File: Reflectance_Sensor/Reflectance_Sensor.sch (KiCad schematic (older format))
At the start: 9 parts, among them Q1 Phototransistor, Q2 Phototransistor

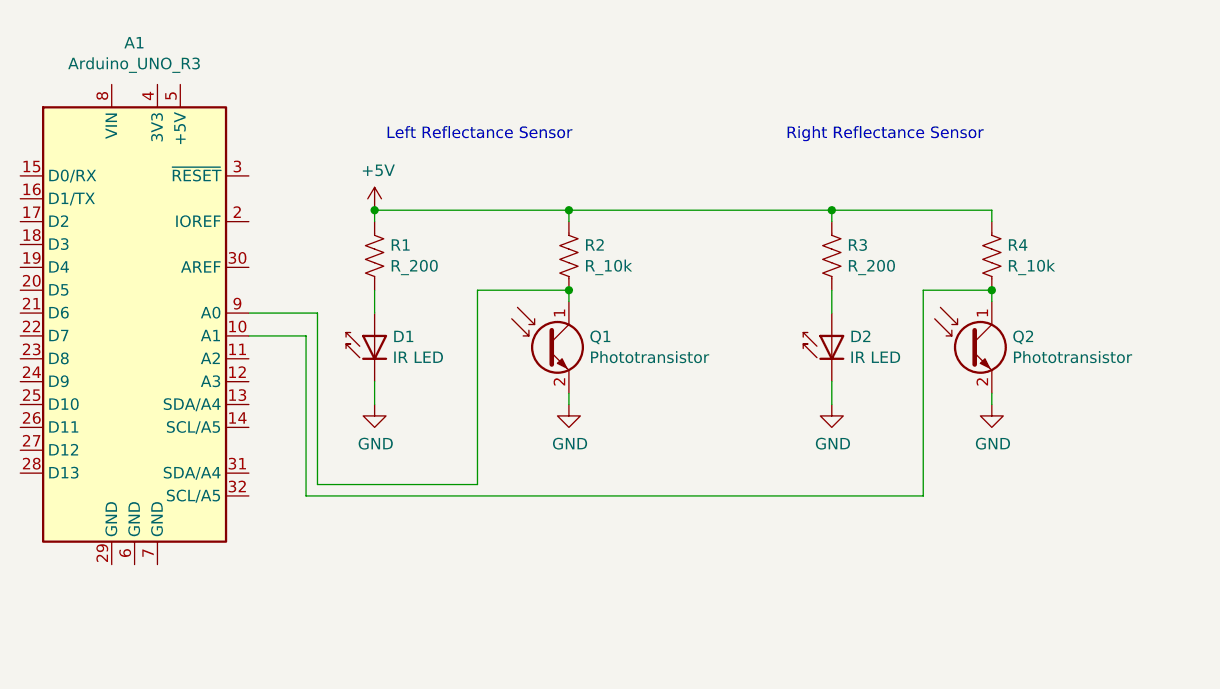
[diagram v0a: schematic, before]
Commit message: Added Motors To diagram
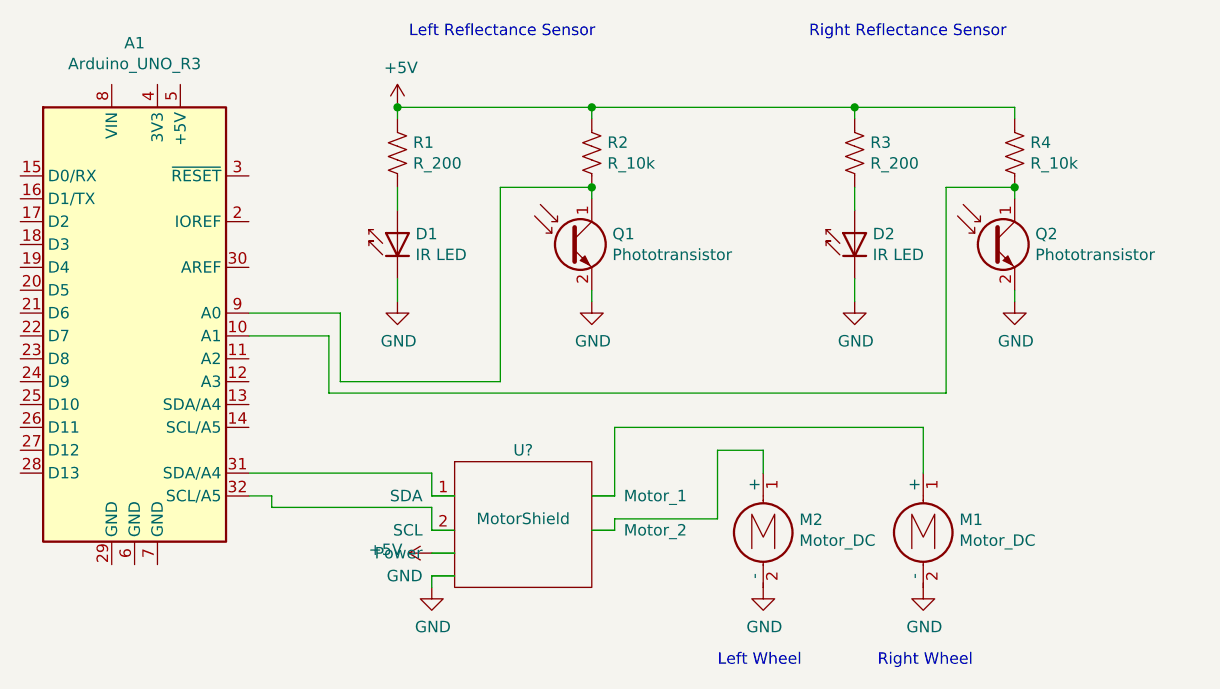
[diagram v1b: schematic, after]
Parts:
- added M1, M2: Motor_DC, symbol Motor:Motor_DC
- added U?: MotorShield, symbol block_diagram_parts:MotorShield
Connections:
- net +5V: now also U?.~ (Power)
- net GND: now also M1.2 (-), M2.2 (-), U?.~ (Power)
- net at A1.31 (SDA/A4): now also U?.1 (SDA)
- net at A1.32 (SCL/A5): now also U?.2 (SCL)
- new net: M2.1 (+), U?.~ (Power)
- new net: M1.1 (+), U?.~ (Power)
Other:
- note added: "Left Wheel"
- note added: "Right Wheel"
- moved on the sheet: D1, D2, Q1, Q2, R1, R2, R3, R4

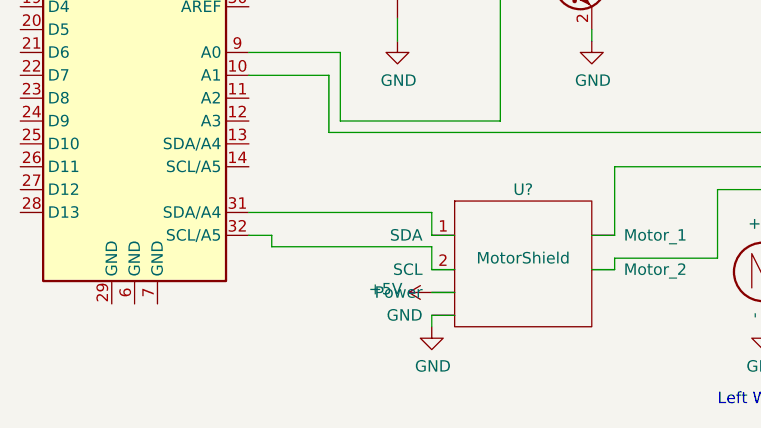
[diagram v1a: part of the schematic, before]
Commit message: Fixed shield power value
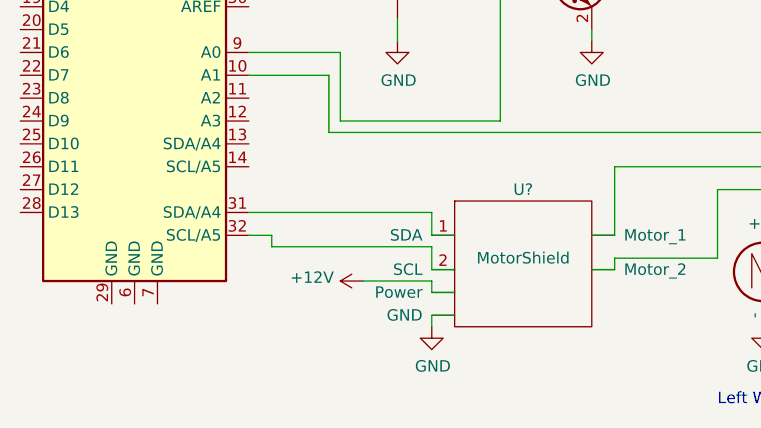
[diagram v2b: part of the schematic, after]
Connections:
- net +5V: no longer U?.~ (Power)
- new net +12V: U?.~ (Power)
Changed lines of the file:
@@
 Wire Wire Line
 	3200 3000 3550 3000
-$Comp
-L block_diagram_parts:MotorShield U?
-U 1 1 6172772E
-P 4400 3650
-F 0 "U?" H 4400 3800 50  0000 C CNN
-F 1 "MotorShield" H 4400 3500 50  0000 C CNN
-F 2 "" H 4400 3650 50  0001 C CNN
-F 3 "" H 4400 3650 50  0001 C CNN
-	1    4400 3650
-	1    0    0    -1
-$EndComp
 Wire Wire Line
 	4100 3850 4000 3850
@@
 	1    5450 3800
 	1    0    0    -1
-$EndComp
-$Comp
-L power:+5V #PWR?
-U 1 1 6172CB26
-P 4000 3950
-F 0 "#PWR?" H 4000 3800 50  0001 C CNN
-F 1 "+5V" V 4015 4078 50  0000 L CNN
-F 2 "" H 4000 3950 50  0001 C CNN
-F 3 "" H 4000 3950 50  0001 C CNN
-	1    4000 3950
-	0    -1   -1   0
 $EndComp
 Wire Wire Line
@@
 Text Notes 5950 4450 0    50   ~ 0
 Right Wheel
+$Comp
+L block_diagram_parts:MotorShield U?
+U 1 1 6172772E
+P 4400 3650
+F 0 "U?" H 4400 3800 50  0000 C CNN
+F 1 "MotorShield" H 4400 3500 50  0000 C CNN
+F 2 "" H 4400 3650 50  0001 C CNN
+F 3 "" H 4400 3650 50  0001 C CNN
+	1    4400 3650
+	1    0    0    -1
+$EndComp
+Wire Wire Line
+	3700 3900 4000 3900
+Wire Wire Line
+	4000 3900 4000 3950
+$Comp
+L power:+12V #PWR?
+U 1 1 61741886
+P 3700 3900
+F 0 "#PWR?" H 3700 3750 50  0001 C CNN
+F 1 "+12V" V 3715 4028 50  0000 L CNN
+F 2 "" H 3700 3900 50  0001 C CNN
+F 3 "" H 3700 3900 50  0001 C CNN
+	1    3700 3900
+	0    -1   -1   0
+$EndComp
 $EndSCHEMATC
